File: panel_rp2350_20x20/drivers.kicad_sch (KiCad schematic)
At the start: 88 parts, among them U10 UCC27517, U11 UCC27517, U12 UCC27517, U13 UCC27517, U14 UCC27517, U15 UCC27517, U16 UCC27517, U17 UCC27517, U18 UCC27517, U19 UCC27517, U20 UCC27517, U21 UCC27517, U22 UCC27517, U23 UCC27517, U24 UCC27517, U25 UCC27517, U26 UCC27517, U27 UCC27517, U28 UCC27517, U29 UCC27517, U3 UCC27517, U30 UCC27517, U31 UCC27517, U32 UCC27517, U33 UCC27517, U34 UCC27517, U35 UCC27517, U36 UCC27517, U37 UCC27517, U38 UCC27517, U4 UCC27517, U40 UCC27517, U41 UCC27517, U42 UCC27517, U43 UCC27517, U5 UCC27517, U6 UCC27517, U7 UCC27517, U8 UCC27517, U9 UCC27517

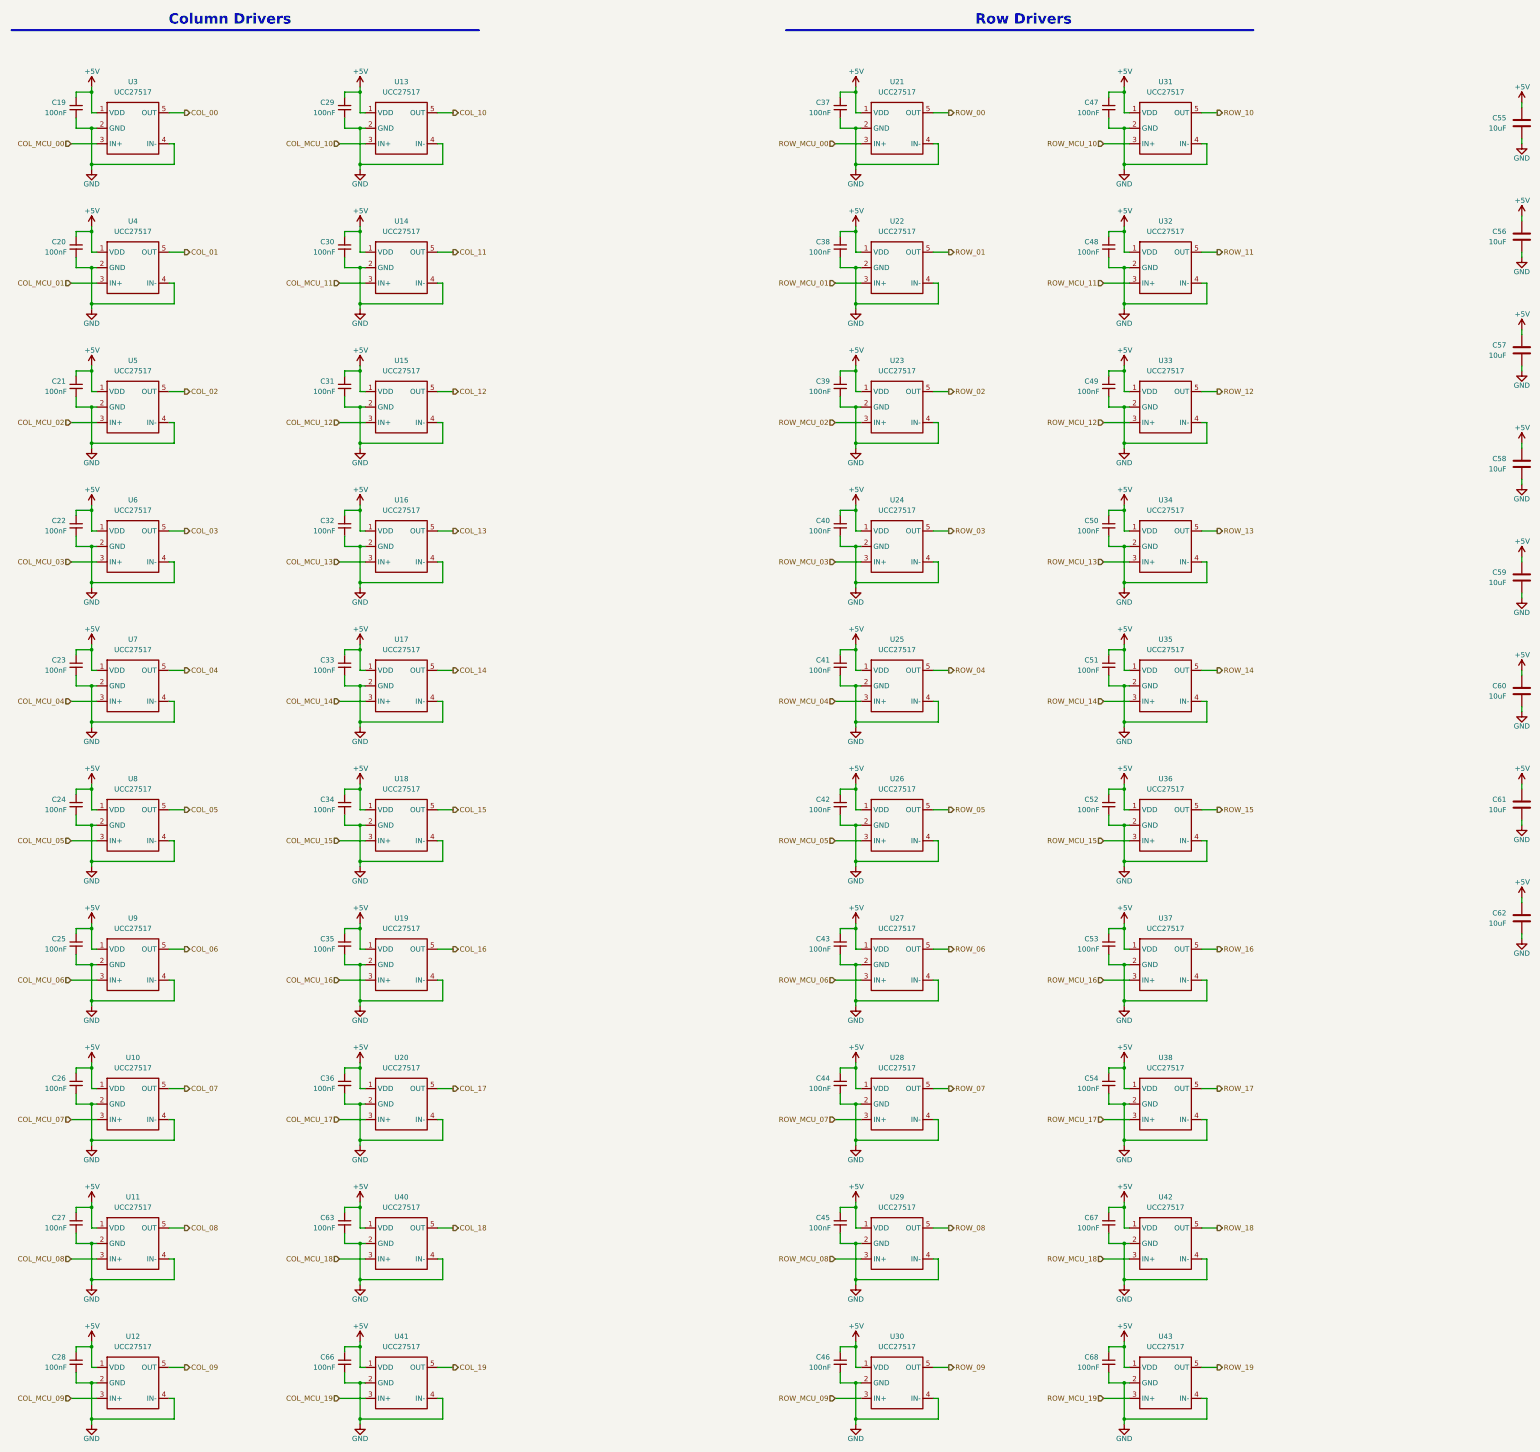
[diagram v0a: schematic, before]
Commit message: More work on rp2350 20x20 panel.
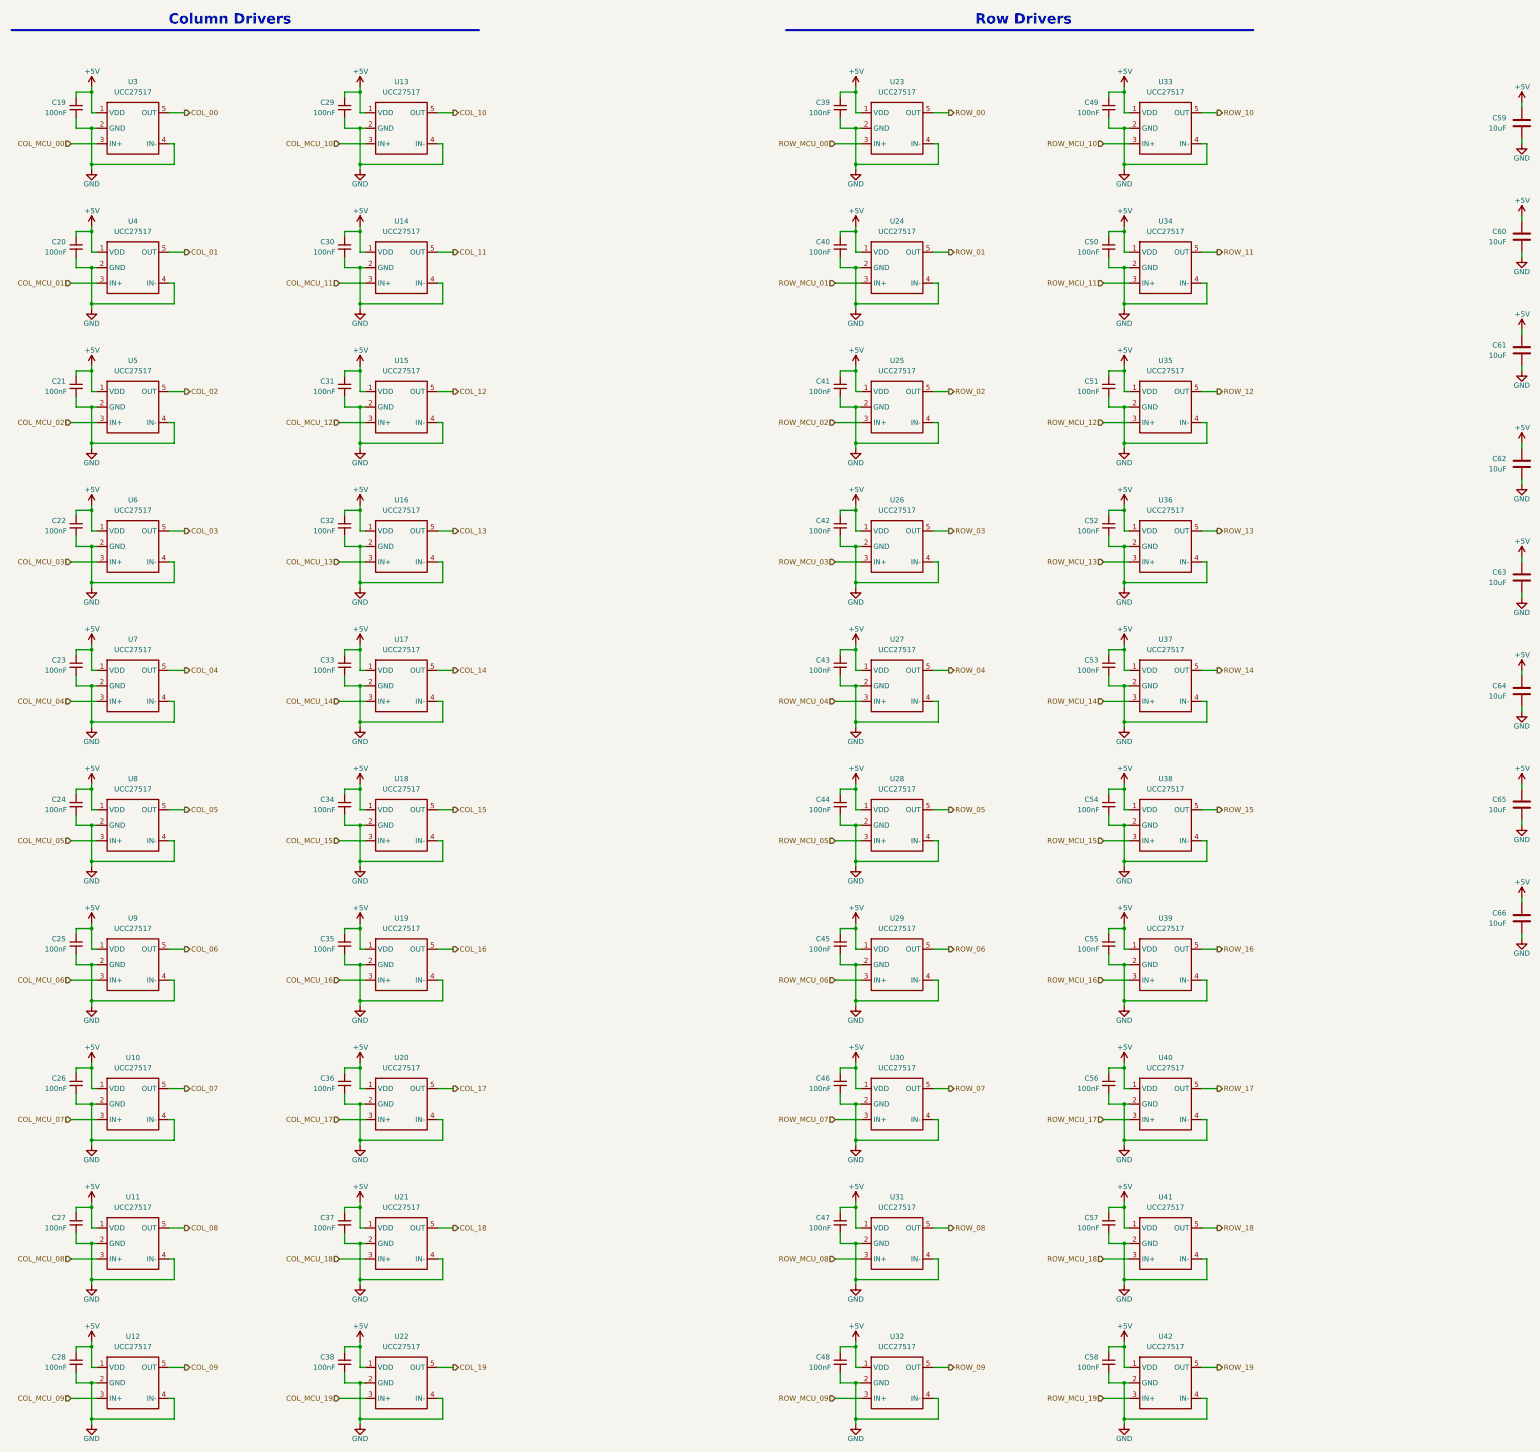
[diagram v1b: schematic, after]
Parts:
- renumbered C63 to C37, C66 to C38, C37 to C39, C38 to C40, C39 to C41, C40 to C42, C41 to C43, C42 to C44, C43 to C45, C44 to C46, C45 to C47, C46 to C48, C47 to C49, C48 to C50, C49 to C51, C50 to C52, C51 to C53, C52 to C54, C53 to C55, C54 to C56, C67 to C57, C68 to C58, C55 to C59, C56 to C60, C57 to C61, C58 to C62, C59 to C63, C60 to C64, C61 to C65, C62 to C66, U40 to U21, U41 to U22, U21 to U23, U22 to U24, U23 to U25, U24 to U26, U25 to U27, U26 to U28, U27 to U29, U28 to U30, U29 to U31, U30 to U32, U31 to U33, U32 to U34, U33 to U35, U34 to U36, U35 to U37, U36 to U38, U37 to U39, U38 to U40, U42 to U41, U43 to U42

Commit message: Work on layout for rp2350 20x20 array panels.
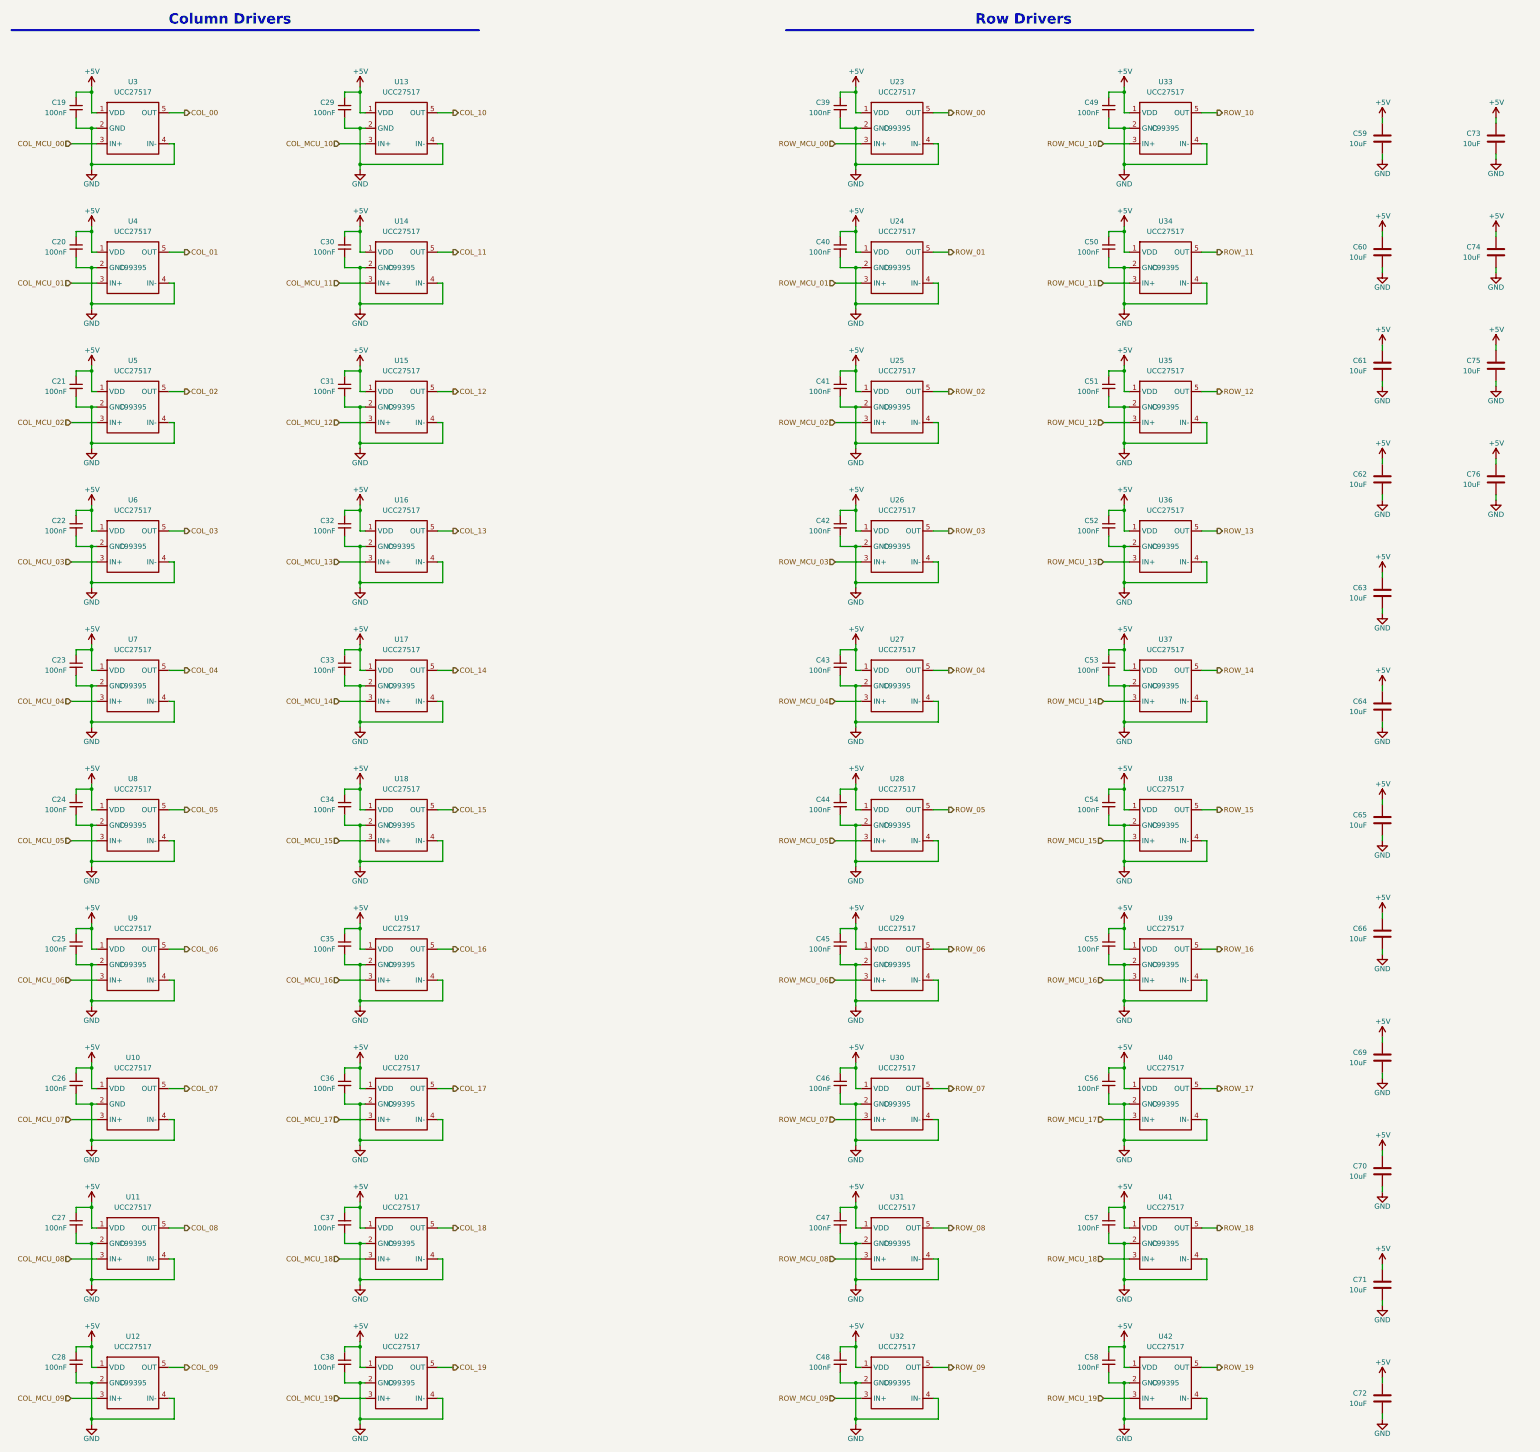
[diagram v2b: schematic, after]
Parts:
- added C69, C70, C71, C72, C73, C74, C75, C76: 10uF, Capacitor_SMD:C_0402_1005Metric, symbol Device:C
- U10, U11, U12, U13, U14, U15, U16, U17, U18, U19, U20, U21, U22, U23, U24, U25, U26, U27, U28, U29, U3, U30, U31, U32, U33, U34, U35, U36, U37, U38, U39, U4, U40, U41, U42, U5, U6, U7, U8, U9: LCSC Part # (none) -> C99395
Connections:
- net +5V: now also C69.1, C70.1, C71.1, C72.1, C73.1, C74.1, C75.1, C76.1
- net GND: now also C69.2, C70.2, C71.2, C72.2, C73.2, C74.2, C75.2, C76.2
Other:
- moved on the sheet: C59, C60, C61, C62, C63, C64, C65, C66

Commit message: Worked on fab files.
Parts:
- C19, C20, C21, C22, C23, C24, C25, C26, C27, C28, C29, C30, C31, C32, C33, C34, C35, C36, C37, C38, C39, C40, C41, C42, C43, C44, C45, C46, C47, C48, C49, C50, C51, C52, C53, C54, C55, C56, C57, C58: LCSC Part # (none) -> C76939
